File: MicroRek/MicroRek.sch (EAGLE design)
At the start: 13 parts

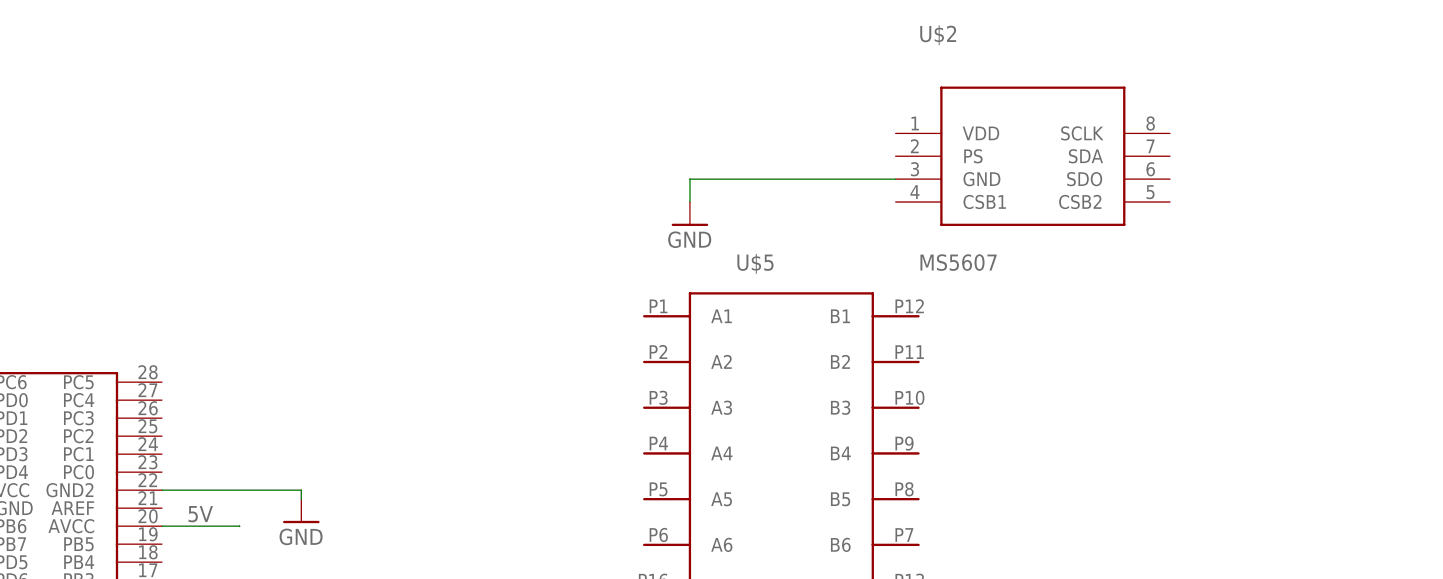
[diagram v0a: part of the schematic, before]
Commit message: Wired Barometer
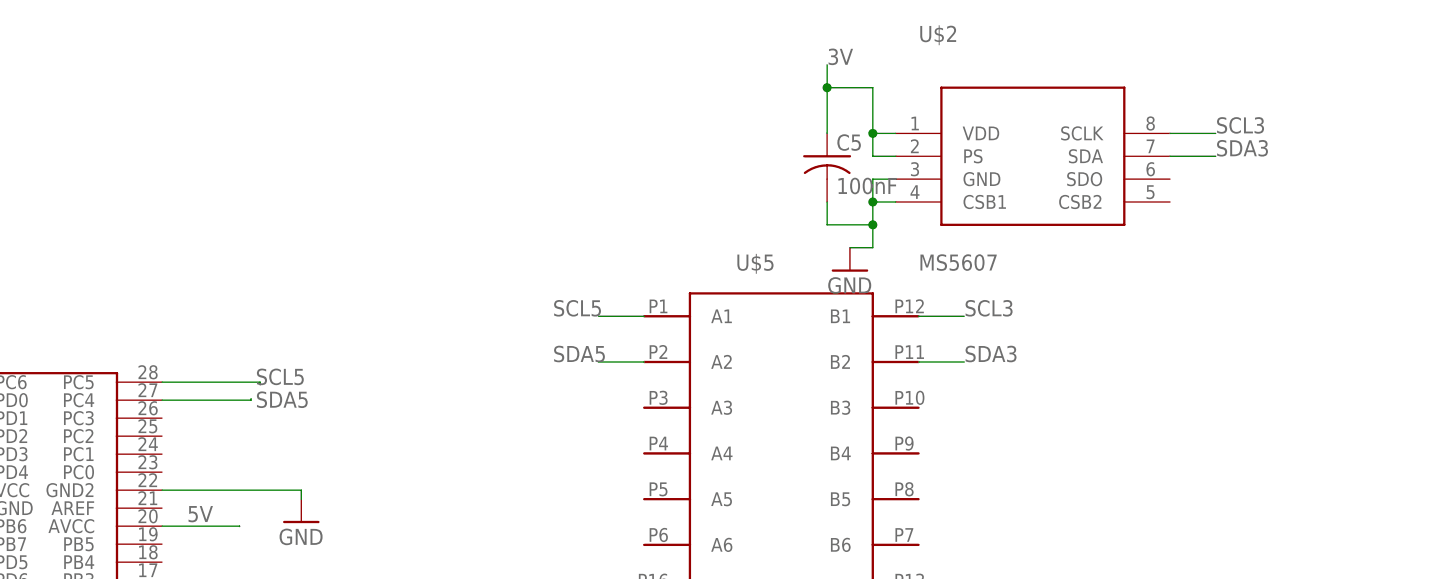
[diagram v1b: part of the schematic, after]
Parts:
- added C5: 100nF, resistor:C-US025-024X044
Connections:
- new net SCL3: U$2.SCLK, U$5.B1
- new net SCL5: U$1.PC5, U$5.A1
- new net SDA3: U$2.SDA, U$5.B2
- new net SDA5: U$1.PC4, U$5.A2
- net 3V: now also C5.1, U$2.PS, U$2.VDD
- net GND: now also C5.2, U$2.CSB1
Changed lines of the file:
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@@
 <part name="C3" library="resistor" library_urn="urn:adsk.eagle:library:348" deviceset="C-US" device="025-024X044" package3d_urn="urn:adsk.eagle:package:26149/1"/>
 <part name="GND13" library="supply1" library_urn="urn:adsk.eagle:library:371" deviceset="GND" device=""/>
+<part name="C5" library="resistor" library_urn="urn:adsk.eagle:library:348" deviceset="C-US" device="025-024X044" package3d_urn="urn:adsk.eagle:package:26149/1" value="100nF"/>
 </parts>
 <sheets>
@@
 <instance part="C2" gate="G$1" x="165.1" y="-73.66"/>
 <instance part="C3" gate="G$1" x="218.44" y="-71.12"/>
-<instance part="GND13" gate="1" x="144.78" y="58.42"/>
+<instance part="GND13" gate="1" x="162.56" y="53.34"/>
+<instance part="C5" gate="G$1" x="160.02" y="66.04"/>
 </instances>
 <busses>
@@
 <segment>
 <pinref part="U$2" gate="G$1" pin="GND"/>
-<wire x1="167.64" y1="63.5" x2="144.78" y2="63.5" width="0.1524" layer="91"/>
+<wire x1="167.64" y1="63.5" x2="165.1" y2="63.5" width="0.1524" layer="91"/>
+<wire x1="165.1" y1="63.5" x2="165.1" y2="60.96" width="0.1524" layer="91"/>
 <pinref part="GND13" gate="1" pin="GND"/>
-<wire x1="144.78" y1="63.5" x2="144.78" y2="60.96" width="0.1524" layer="91"/>
+<wire x1="165.1" y1="60.96" x2="165.1" y2="58.42" width="0.1524" layer="91"/>
+<wire x1="165.1" y1="58.42" x2="165.1" y2="55.88" width="0.1524" layer="91"/>
+<wire x1="165.1" y1="55.88" x2="162.56" y2="55.88" width="0.1524" layer="91"/>
+<pinref part="C5" gate="G$1" pin="2"/>
+<wire x1="165.1" y1="58.42" x2="160.02" y2="58.42" width="0.1524" layer="91"/>
+<wire x1="160.02" y1="58.42" x2="160.02" y2="60.96" width="0.1524" layer="91"/>
+<junction x="165.1" y="58.42"/>
+<pinref part="U$2" gate="G$1" pin="CSB1"/>
+<wire x1="167.64" y1="60.96" x2="165.1" y2="60.96" width="0.1524" layer="91"/>
+<junction x="165.1" y="60.96"/>
 </segment>
 </net>
@@
 <wire x1="218.44" y1="-60.96" x2="218.44" y2="-68.58" width="0.1524" layer="91"/>
 </segment>
+<segment>
+<pinref part="U$2" gate="G$1" pin="PS"/>
+<wire x1="167.64" y1="66.04" x2="165.1" y2="66.04" width="0.1524" layer="91"/>
+<wire x1="165.1" y1="66.04" x2="165.1" y2="68.58" width="0.1524" layer="91"/>
+<pinref part="U$2" gate="G$1" pin="VDD"/>
+<wire x1="167.64" y1="68.58" x2="165.1" y2="68.58" width="0.1524" layer="91"/>
+<wire x1="165.1" y1="68.58" x2="165.1" y2="73.66" width="0.1524" layer="91"/>
+<wire x1="165.1" y1="73.66" x2="160.02" y2="73.66" width="0.1524" layer="91"/>
+<wire x1="160.02" y1="73.66" x2="160.02" y2="76.2" width="0.1524" layer="91"/>
+<junction x="165.1" y="68.58"/>
+<pinref part="C5" gate="G$1" pin="1"/>
+<wire x1="160.02" y1="68.58" x2="160.02" y2="73.66" width="0.1524" layer="91"/>
+<junction x="160.02" y="73.66"/>
+<label x="160.02" y="76.2" size="1.778" layer="95"/>
+</segment>
 </net>
 <net name="N$3" class="0">
@@
 </segment>
 </net>
+<net name="SDA5" class="0">
+<segment>
+<pinref part="U$1" gate="G$1" pin="PC4"/>
+<wire x1="86.12" y1="38.94" x2="96.012" y2="38.94" width="0.1524" layer="91"/>
+<wire x1="96.012" y1="38.94" x2="96.012" y2="39.116" width="0.1524" layer="91"/>
+<label x="96.52" y="38.1" size="1.778" layer="95"/>
+</segment>
+<segment>
+<pinref part="U$5" gate="G$1" pin="A2"/>
+<wire x1="139.7" y1="43.18" x2="134.62" y2="43.18" width="0.1524" layer="91"/>
+<label x="129.54" y="43.18" size="1.778" layer="95"/>
+</segment>
+</net>
+<net name="SCL5" class="0">
+<segment>
+<pinref part="U$1" gate="G$1" pin="PC5"/>
+<wire x1="86.12" y1="40.94" x2="97.028" y2="40.94" width="0.1524" layer="91"/>
+<wire x1="97.028" y1="40.94" x2="97.028" y2="40.64" width="0.1524" layer="91"/>
+<label x="96.52" y="40.64" size="1.778" layer="95"/>
+</segment>
+<segment>
+<pinref part="U$5" gate="G$1" pin="A1"/>
+<wire x1="139.7" y1="48.26" x2="134.62" y2="48.26" width="0.1524" layer="91"/>
+<label x="129.54" y="48.26" size="1.778" layer="95"/>
+</segment>
+</net>
+<net name="SDA3" class="0">
+<segment>
+<pinref part="U$5" gate="G$1" pin="B2"/>
+<wire x1="170.18" y1="43.18" x2="175.26" y2="43.18" width="0.1524" layer="91"/>
+<label x="175.26" y="43.18" size="1.778" layer="95"/>
+</segment>
+<segment>
+<pinref part="U$2" gate="G$1" pin="SDA"/>
+<wire x1="198.12" y1="66.04" x2="203.2" y2="66.04" width="0.1524" layer="91"/>
+<label x="203.2" y="66.04" size="1.778" layer="95"/>
+</segment>
+</net>
+<net name="SCL3" class="0">
+<segment>
+<pinref part="U$5" gate="G$1" pin="B1"/>
+<wire x1="170.18" y1="48.26" x2="175.26" y2="48.26" width="0.1524" layer="91"/>
+<label x="175.26" y="48.26" size="1.778" layer="95"/>
+</segment>
+<segment>
+<pinref part="U$2" gate="G$1" pin="SCLK"/>
+<wire x1="198.12" y1="68.58" x2="203.2" y2="68.58" width="0.1524" layer="91"/>
+<label x="203.2" y="68.58" size="1.778" layer="95"/>
+</segment>
+</net>
